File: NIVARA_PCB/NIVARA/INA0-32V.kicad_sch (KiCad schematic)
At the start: 0 parts

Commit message: avance
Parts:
- added C7: 100nF, PCM_Capacitor_SMD_AKL:C_0603_1608Metric, symbol PCM_Capacitor_AKL:C_0603
- added R42: 10K, PCM_Resistor_SMD_AKL:R_0603_1608Metric, symbol PCM_Resistor_AKL:R_0603
- added R6: 1K, PCM_Resistor_SMD_AKL:R_1206_3216Metric_Pad1.30x1.75mm_HandSolder, symbol PCM_Resistor_AKL:R_0603
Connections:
- net IN_1: now also R42.1
- net OUT_1: now also C7.2, R42.2, R6.2
- new net GND: C7.1, R6.1
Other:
- note added: "0-32V"

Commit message: ACTUALIZACION
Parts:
- C7: PART NUMBERT (none) -> CC0603KRX7R9BB104
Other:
- moved on the sheet: C7
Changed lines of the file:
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@@
 	)
 	(junction
-		(at 46.99 44.45)
+		(at 44.45 44.45)
 		(diameter 0)
 		(color 0 0 0 0)
@@
 	(wire
 		(pts
-			(xy 34.29 44.45) (xy 46.99 44.45)
-		)
-		(stroke
-			(width 0)
-			(type default)
-		)
-	)
-	(wire
-		(pts
-			(xy 46.99 44.45) (xy 52.07 44.45)
-		)
-		(stroke
-			(width 0)
-			(type default)
-		)
-	)
-	(wire
-		(pts
-			(xy 46.99 57.15) (xy 46.99 52.07)
+			(xy 34.29 44.45) (xy 44.45 44.45)
+		)
+		(stroke
+			(width 0)
+			(type default)
+		)
+	)
+	(wire
+		(pts
+			(xy 44.45 52.07) (xy 44.45 57.15)
+		)
+		(stroke
+			(width 0)
+			(type default)
+		)
+	)
+	(wire
+		(pts
+			(xy 44.45 44.45) (xy 58.42 44.45)
 		)
 		(stroke
@@
 	(hierarchical_label "OUT_1"
 		(shape output)
-		(at 52.07 44.45 0)
+		(at 58.42 44.45 0)
 		(effects
 			(font
@@
 	(symbol
 		(lib_id "power:GND")
-		(at 46.99 57.15 0)
+		(at 44.45 57.15 0)
 		(unit 1)
 		(exclude_from_sim no)
@@
 		(fields_autoplaced yes)
 		(property "Reference" "#PWR018"
-			(at 46.99 63.5 0)
+			(at 44.45 63.5 0)
 			(effects
 				(font
@@
 		)
 		(property "Value" "GND"
-			(at 46.99 62.23 0)
+			(at 44.45 62.23 0)
 			(effects
 				(font
@@
 		)
 		(property "Footprint" ""
-			(at 46.99 57.15 0)
+			(at 44.45 57.15 0)
 			(effects
 				(font
@@
 		)
 		(property "Datasheet" ""
-			(at 46.99 57.15 0)
+			(at 44.45 57.15 0)
 			(effects
 				(font
@@
 		)
 		(property "Description" "Power symbol creates a global label with name \"GND\" , ground"
-			(at 46.99 57.15 0)
+			(at 44.45 57.15 0)
 			(effects
 				(font
@@
 	(symbol
 		(lib_id "PCM_Capacitor_AKL:C_0603")
-		(at 46.99 48.26 180)
+		(at 44.45 48.26 180)
 		(unit 1)
 		(exclude_from_sim no)
@@
 		(dnp no)
 		(property "Reference" "C7"
-			(at 45.72 50.8 90)
+			(at 43.18 50.8 90)
 			(effects
 				(font
@@
 		)
 		(property "Value" "100nF"
-			(at 50.8 44.45 90)
+			(at 48.26 44.45 90)
 			(effects
 				(font
@@
 		)
 		(property "Footprint" "PCM_Capacitor_SMD_AKL:C_0603_1608Metric"
-			(at 46.0248 44.45 0)
+			(at 43.4848 44.45 0)
 			(effects
 				(font
@@
 		)
 		(property "Datasheet" "~"
-			(at 46.99 48.26 0)
+			(at 44.45 48.26 0)
 			(effects
 				(font
@@
 		)
 		(property "Description" "SMD 0603 MLCC capacitor, Alternate KiCad Library"
-			(at 46.99 48.26 0)
-			(effects
-				(font
-					(size 1.27 1.27)
-				)
-				(hide yes)
-			)
-		)
-		(property "PART NUMBERT" ""
-			(at 46.99 48.26 0)
-			(effects
-				(font
+			(at 44.45 48.26 0)
+			(effects
+				(font
+					(size 1.27 1.27)
+				)
+				(hide yes)
+			)
+		)
+		(property "PART NUMBERT" "CC0603KRX7R9BB104"
+			(at 44.45 48.26 0)
+			(effects
+				(font

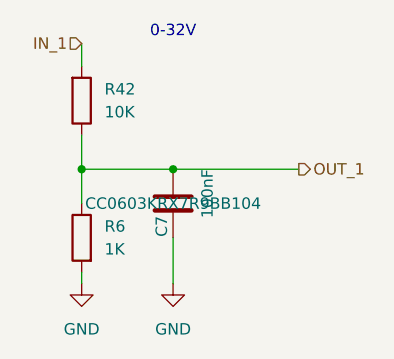
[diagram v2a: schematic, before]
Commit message: Se organizaron componentes en el area de PCB
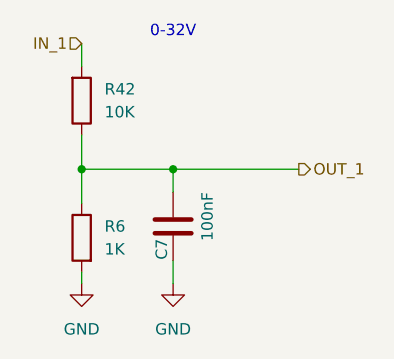
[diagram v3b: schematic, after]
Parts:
- R6: footprint PCM_Resistor_SMD_AKL:R_1206_3216Metric_Pad1.30x1.75mm_HandSolder -> PCM_Resistor_SMD_AKL:R_0603_1608Metric; PART NUMBERT CRCW12061K00FKEAHP -> RC0603FR-071KL
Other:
- moved on the sheet: C7
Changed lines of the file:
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@@
 	(wire
 		(pts
-			(xy 44.45 52.07) (xy 44.45 57.15)
+			(xy 44.45 46.99) (xy 44.45 44.45)
+		)
+		(stroke
+			(width 0)
+			(type default)
+		)
+	)
+	(wire
+		(pts
+			(xy 44.45 54.61) (xy 44.45 57.15)
 		)
 		(stroke
@@
 			)
 		)
-		(property "Footprint" "PCM_Resistor_SMD_AKL:R_1206_3216Metric_Pad1.30x1.75mm_HandSolder"
+		(property "Footprint" "PCM_Resistor_SMD_AKL:R_0603_1608Metric"
 			(at 34.29 40.64 0)
 			(effects
@@
 			)
 		)
-		(property "PART NUMBERT" "CRCW12061K00FKEAHP"
+		(property "PART NUMBERT" "RC0603FR-071KL"
 			(at 34.29 52.07 0)
 			(effects
@@
 	(symbol
 		(lib_id "PCM_Capacitor_AKL:C_0603")
-		(at 44.45 48.26 180)
+		(at 44.45 50.8 180)
 		(unit 1)
 		(exclude_from_sim no)
@@
 		(dnp no)
 		(property "Reference" "C7"
-			(at 43.18 50.8 90)
+			(at 43.18 53.34 90)
 			(effects
 				(font
@@
 		)
 		(property "Value" "100nF"
-			(at 48.26 44.45 90)
+			(at 48.26 46.99 90)
 			(effects
 				(font
@@
 		)
 		(property "Footprint" "PCM_Capacitor_SMD_AKL:C_0603_1608Metric"
-			(at 43.4848 44.45 0)
+			(at 43.4848 46.99 0)
 			(effects
 				(font
@@
 		)
 		(property "Datasheet" "~"
-			(at 44.45 48.26 0)
+			(at 44.45 50.8 0)
 			(effects
 				(font
@@
 		)
 		(property "Description" "SMD 0603 MLCC capacitor, Alternate KiCad Library"
-			(at 44.45 48.26 0)
+			(at 44.45 50.8 0)
 			(effects
 				(font
@@
 		)
 		(property "PART NUMBERT" "CC0603KRX7R9BB104"
-			(at 44.45 48.26 0)
-			(effects
-				(font
-					(size 1.27 1.27)
-				)
-			)
-		)
+			(at 44.45 50.8 0)
+			(effects
+				(font
+					(size 1.27 1.27)
+				)
+				(hide yes)
+			)
+		)

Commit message: organizando componentes en la pcb
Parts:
- removed R42: 10K, PCM_Resistor_SMD_AKL:R_0603_1608Metric, symbol PCM_Resistor_AKL:R_0603
- added R18: 2.5K, PCM_Resistor_SMD_AKL:R_0603_1608Metric, symbol PCM_Resistor_AKL:R_0603
- R6: value 1K -> 22K; PART NUMBERT RC0603FR-071KL -> RC0603FR-0722KL
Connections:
- net GND: now also R18.2; no longer R6.1
- net IN_1: now also R6.1
- net OUT_1: now also R18.1
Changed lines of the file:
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@@
 	(wire
 		(pts
-			(xy 34.29 57.15) (xy 34.29 55.88)
-		)
-		(stroke
-			(width 0)
-			(type default)
-		)
-	)
-	(wire
-		(pts
-			(xy 34.29 48.26) (xy 34.29 44.45)
+			(xy 34.29 44.45) (xy 34.29 46.99)
 		)
 		(stroke
@@
 		(pts
 			(xy 44.45 44.45) (xy 58.42 44.45)
+		)
+		(stroke
+			(width 0)
+			(type default)
+		)
+	)
+	(wire
+		(pts
+			(xy 34.29 54.61) (xy 34.29 57.15)
 		)
 		(stroke
@@
 	)
 	(symbol
-		(lib_id "PCM_Resistor_AKL:R_0603")
-		(at 34.29 52.07 180)
-		(unit 1)
-		(exclude_from_sim no)
-		(in_bom yes)
-		(on_board yes)
-		(dnp no)
-		(fields_autoplaced yes)
-		(property "Reference" "R6"
-			(at 36.83 50.7999 0)
-			(effects
-				(font
-					(size 1.27 1.27)
-				)
-				(justify right)
-			)
-		)
-		(property "Value" "1K"
-			(at 36.83 53.3399 0)
-			(effects
-				(font
-					(size 1.27 1.27)
-				)
-				(justify right)
-			)
-		)
-		(property "Footprint" "PCM_Resistor_SMD_AKL:R_0603_1608Metric"
-			(at 34.29 40.64 0)
-			(effects
-				(font
-					(size 1.27 1.27)
-				)
-				(hide yes)
-			)
-		)
-		(property "Datasheet" "~"
-			(at 34.29 52.07 0)
-			(effects
-				(font
-					(size 1.27 1.27)
-				)
-				(hide yes)
-			)
-		)
-		(property "Description" "SMD 0603 Chip Resistor, European Symbol, Alternate KiCad Library"
-			(at 34.29 52.07 0)
-			(effects
-				(font
-					(size 1.27 1.27)
-				)
-				(hide yes)
-			)
-		)
-		(property "PART NUMBERT" "RC0603FR-071KL"
-			(at 34.29 52.07 0)
-			(effects
-				(font
-					(size 1.27 1.27)
-				)
-				(hide yes)
-			)
-		)
-		(pin "2"
-		)
-		(pin "1"
-		)
-		(instances
-			(project "NIVARA"
-				(path "/6298d7d5-28da-40bf-9586-24a8e5c02b82/7ff0dada-fc46-483c-91ad-b264be8c64cf/5f7419b9-a365-44ee-a39a-fe132ae08548"
-					(reference "R6")
-					(unit 1)
-				)
-			)
-		)
-	)
-	(symbol
 		(lib_id "PCM_Capacitor_AKL:C_0603")
 		(at 44.45 50.8 180)
@@
 				(path "/6298d7d5-28da-40bf-9586-24a8e5c02b82/7ff0dada-fc46-483c-91ad-b264be8c64cf/5f7419b9-a365-44ee-a39a-fe132ae08548"
 					(reference "C7")
+					(unit 1)
+				)
+			)
+		)
+	)
+	(symbol
+		(lib_id "PCM_Resistor_AKL:R_0603")
+		(at 34.29 50.8 0)
+		(unit 1)
+		(exclude_from_sim no)
+		(in_bom yes)
+		(on_board yes)
+		(dnp no)
+		(property "Reference" "R18"
+			(at 34.29 52.07 90)
+			(effects
+				(font
+					(size 1.27 1.27)
+				)
+				(justify left)
+			)
+		)
+		(property "Value" "2.5K"
+			(at 33.02 54.61 0)
+			(effects
+				(font
+					(size 1.27 1.27)
+				)
+				(justify left)
+			)
+		)
+		(property "Footprint" "PCM_Resistor_SMD_AKL:R_0603_1608Metric"
+			(at 34.29 62.23 0)
+			(effects
+				(font
+					(size 1.27 1.27)
+				)
+				(hide yes)
+			)
+		)
+		(property "Datasheet" "~"
+			(at 34.29 50.8 0)
+			(effects
+				(font
+					(size 1.27 1.27)
+				)
+				(hide yes)
+			)
+		)
+		(property "Description" "SMD 0603 Chip Resistor, European Symbol, Alternate KiCad Library"
+			(at 34.29 50.8 0)
+			(effects
+				(font
+					(size 1.27 1.27)
+				)
+				(hide yes)
+			)
+		)
+		(property "PART NUMBERT" "FRQ0805F2501TS"
+			(at 34.29 50.8 0)
+			(effects
+				(font
+					(size 1.27 1.27)
+				)
+				(hide yes)
+			)
+		)
+		(pin "1"
+		)
+		(pin "2"
+		)
+		(instances
+			(project "NIVARA"
+				(path "/6298d7d5-28da-40bf-9586-24a8e5c02b82/7ff0dada-fc46-483c-91ad-b264be8c64cf/5f7419b9-a365-44ee-a39a-fe132ae08548"
+					(reference "R18")
 					(unit 1)
 				)
@@
 		(dnp no)
 		(fields_autoplaced yes)
-		(property "Reference" "R42"
+		(property "Reference" "R6"
 			(at 36.83 35.5599 0)
 			(effects
@@
 			)
 		)
-		(property "Value" "10K"
+		(property "Value" "22K"
 			(at 36.83 38.0999 0)
 			(effects
@@
 			)
 		)
-		(property "PART NUMBERT" ""
+		(property "PART NUMBERT" "RC0603FR-0722KL"
 			(at 34.29 36.83 0)
 			(effects
@@
 					(size 1.27 1.27)
 				)
-			)
+				(hide yes)
+			)
+		)
+		(pin "1"
 		)
 		(pin "2"
-		)
-		(pin "1"
 		)
 		(instances
 			(project "NIVARA"
 				(path "/6298d7d5-28da-40bf-9586-24a8e5c02b82/7ff0dada-fc46-483c-91ad-b264be8c64cf/5f7419b9-a365-44ee-a39a-fe132ae08548"
-					(reference "R42")
+					(reference "R6")
 					(unit 1)
 				)
